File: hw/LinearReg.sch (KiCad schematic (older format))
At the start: 2 parts

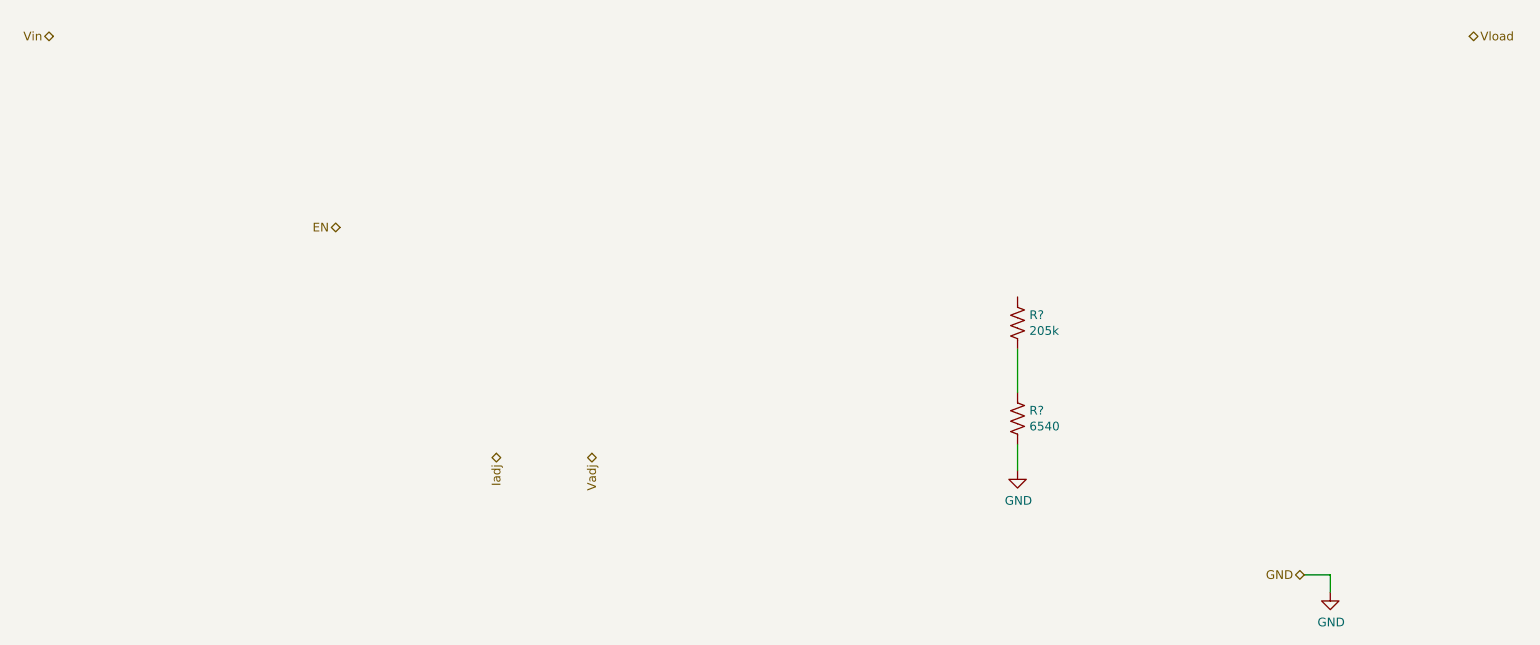
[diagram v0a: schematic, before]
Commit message: Primary SW component selection
selected some components for primary switcher, added AuxOut block, dropped down primary linear reg IC
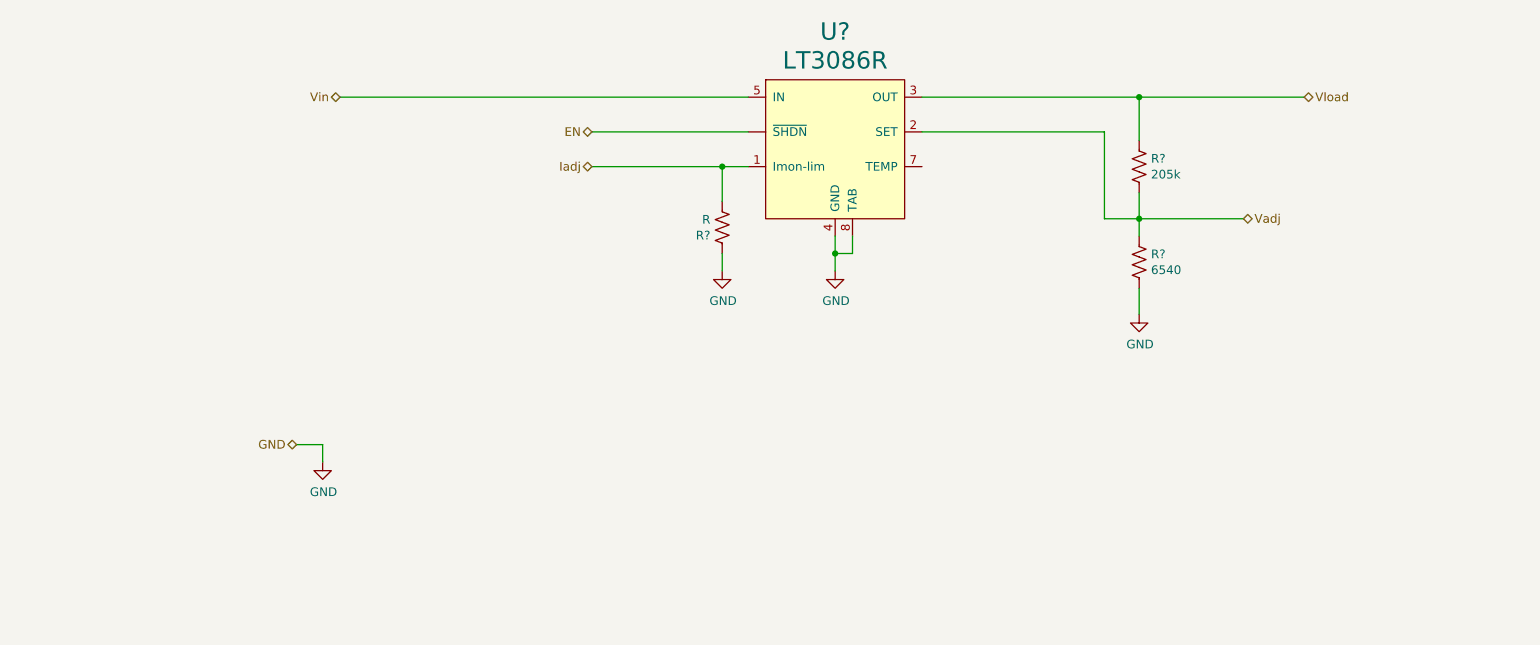
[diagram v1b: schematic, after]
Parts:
- added R?: R, Resistor_SMD:R_0603_1608Metric, symbol Device:R_US
- added U?: LT3086R, symbol RDSmith:LT3086R
- R? (x2): footprint (none) -> Resistor_SMD:R_0603_1608Metric
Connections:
- net EN: now also U?.~ (~SHDN)
- net GND: now also R?.1, U?.4 (GND), U?.8 (TAB)
- net Iadj: now also R?.2, U?.1 (Imon-lim)
- net Vadj: now also R?.1, R?.2, U?.2 (SET)
- net Vin: now also U?.5 (IN)
- net Vload: now also R?.1, U?.3 (OUT)
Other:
- moved on the sheet: R?
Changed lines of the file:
@@
 $Descr A4 11693 8268
 encoding utf-8
-Sheet 5 6
+Sheet 5 7
 Title ""
 Date ""
@@
 Comment4 ""
 $EndDescr
-Text HLabel 8750 4900 0    50   BiDi ~ 0
+Text HLabel 2950 4150 0    50   BiDi ~ 0
 GND
-Text HLabel 1550 1800 0    50   BiDi ~ 0
+Text HLabel 3200 2150 0    50   BiDi ~ 0
 Vin
-Text HLabel 9700 1800 2    50   BiDi ~ 0
+Text HLabel 8750 2150 2    50   BiDi ~ 0
 Vload
-Text HLabel 4650 4200 3    50   BiDi ~ 0
+Text HLabel 8400 2850 2    50   BiDi ~ 0
 Vadj
-Text HLabel 4100 4200 3    50   BiDi ~ 0
+Text HLabel 4650 2550 0    50   BiDi ~ 0
 Iadj
-Text HLabel 3200 2900 0    50   BiDi ~ 0
+Text HLabel 4650 2350 0    50   BiDi ~ 0
 EN
 $Comp
 L Device:R_US R?
 U 1 1 5E99EF91
-P 7100 3450
-F 0 "R?" H 7168 3496 50  0000 L CNN
-F 1 "205k" H 7168 3405 50  0000 L CNN
-F 2 "" V 7140 3440 50  0001 C CNN
-F 3 "~" H 7100 3450 50  0001 C CNN
-	1    7100 3450
+P 7800 2550
+F 0 "R?" H 7868 2596 50  0000 L CNN
+F 1 "205k" H 7868 2505 50  0000 L CNN
+F 2 "Resistor_SMD:R_0603_1608Metric" V 7840 2540 50  0001 C CNN
+F 3 "~" H 7800 2550 50  0001 C CNN
+	1    7800 2550
 	1    0    0    -1
 $EndComp
@@
 L Device:R_US R?
 U 1 1 5E99EFE9
-P 7100 4000
-F 0 "R?" H 7168 4046 50  0000 L CNN
-F 1 "6540" H 7168 3955 50  0000 L CNN
-F 2 "" V 7140 3990 50  0001 C CNN
-F 3 "~" H 7100 4000 50  0001 C CNN
-	1    7100 4000
+P 7800 3100
+F 0 "R?" H 7868 3146 50  0000 L CNN
+F 1 "6540" H 7868 3055 50  0000 L CNN
+F 2 "Resistor_SMD:R_0603_1608Metric" V 7840 3090 50  0001 C CNN
+F 3 "~" H 7800 3100 50  0001 C CNN
+	1    7800 3100
 	1    0    0    -1
 $EndComp
 Wire Wire Line
-	7100 3600 7100 3850
+	7800 2700 7800 2850
 $Comp
 L power:GND #PWR?
 U 1 1 5E99F06A
-P 8900 5000
-F 0 "#PWR?" H 8900 4750 50  0001 C CNN
-F 1 "GND" H 8905 4827 50  0000 C CNN
-F 2 "" H 8900 5000 50  0001 C CNN
-F 3 "" H 8900 5000 50  0001 C CNN
-	1    8900 5000
+P 3100 4250
+F 0 "#PWR?" H 3100 4000 50  0001 C CNN
+F 1 "GND" H 3105 4077 50  0000 C CNN
+F 2 "" H 3100 4250 50  0001 C CNN
+F 3 "" H 3100 4250 50  0001 C CNN
+	1    3100 4250
 	1    0    0    -1
 $EndComp
 Wire Wire Line
-	8900 5000 8900 4900
+	3100 4250 3100 4150
 Wire Wire Line
-	8900 4900 8750 4900
+	3100 4150 2950 4150
 $Comp
 L power:GND #PWR?
 U 1 1 5E99F090
-P 7100 4300
-F 0 "#PWR?" H 7100 4050 50  0001 C CNN
-F 1 "GND" H 7105 4127 50  0000 C CNN
-F 2 "" H 7100 4300 50  0001 C CNN
-F 3 "" H 7100 4300 50  0001 C CNN
-	1    7100 4300
+P 7800 3400
+F 0 "#PWR?" H 7800 3150 50  0001 C CNN
+F 1 "GND" H 7805 3227 50  0000 C CNN
+F 2 "" H 7800 3400 50  0001 C CNN
+F 3 "" H 7800 3400 50  0001 C CNN
+	1    7800 3400
 	1    0    0    -1
 $EndComp
 Wire Wire Line
-	7100 4300 7100 4150
+	7800 3400 7800 3250
+$Comp
+L RDSmith:LT3086R U?
+U 1 1 5EB6D3E5
+P 6050 2450
+F 0 "U?" H 6050 3127 100 0000 C CNN
+F 1 "LT3086R" H 6050 2961 100 0000 C CNN
+F 2 "" H 6050 2450 100 0001 C CNN
+F 3 "" H 6050 2450 100 0001 C CNN
+	1    6050 2450
+	1    0    0    -1
+$EndComp
+Wire Wire Line
+	8750 2150 7800 2150
+$Comp
+L power:GND #PWR?
+U 1 1 5EB6D471
+P 6050 3150
+F 0 "#PWR?" H 6050 2900 50  0001 C CNN
+F 1 "GND" H 6055 2977 50  0000 C CNN
+F 2 "" H 6050 3150 50  0001 C CNN
+F 3 "" H 6050 3150 50  0001 C CNN
+	1    6050 3150
+	1    0    0    -1
+$EndComp
+Wire Wire Line
+	6050 3150 6050 3050
+Wire Wire Line
+	6150 2950 6150 3050
+Wire Wire Line
+	6150 3050 6050 3050
+Connection ~ 6050 3050
+Wire Wire Line
+	6050 3050 6050 2950
+Wire Wire Line
+	3200 2150 5550 2150
+Wire Wire Line
+	4650 2350 5550 2350
+Wire Wire Line
+	7800 2400 7800 2150
+Connection ~ 7800 2150
+Wire Wire Line
+	7800 2150 6550 2150
+Wire Wire Line
+	6550 2350 7600 2350
+Wire Wire Line
+	7600 2350 7600 2850
+Wire Wire Line
+	7600 2850 7800 2850
+Connection ~ 7800 2850
+Wire Wire Line
+	7800 2850 7800 2950
+Wire Wire Line
+	8400 2850 7800 2850
+$Comp
+L Device:R_US R?
+U 1 1 5EB6DF74
+P 5400 2900
+F 0 "R?" H 5468 2946 50  0000 L CNN
+F 1 "R" H 5468 2855 50  0000 L CNN
+F 2 "Resistor_SMD:R_0603_1608Metric" V 5440 2890 50  0001 C CNN
+F 3 "~" H 5400 2900 50  0001 C CNN
+	1    5400 2900
+	-1   0    0    1
+$EndComp
+Wire Wire Line
+	5400 2750 5400 2550
+Wire Wire Line
+	5400 2550 5550 2550
+Wire Wire Line
+	4650 2550 5400 2550
+Connection ~ 5400 2550
+$Comp
+L power:GND #PWR?
+U 1 1 5EB6E351
+P 5400 3150
+F 0 "#PWR?" H 5400 2900 50  0001 C CNN
+F 1 "GND" H 5405 2977 50  0000 C CNN
+F 2 "" H 5400 3150 50  0001 C CNN
+F 3 "" H 5400 3150 50  0001 C CNN
+	1    5400 3150
+	1    0    0    -1
+$EndComp
+Wire Wire Line
+	5400 3150 5400 3050
 $EndSCHEMATC

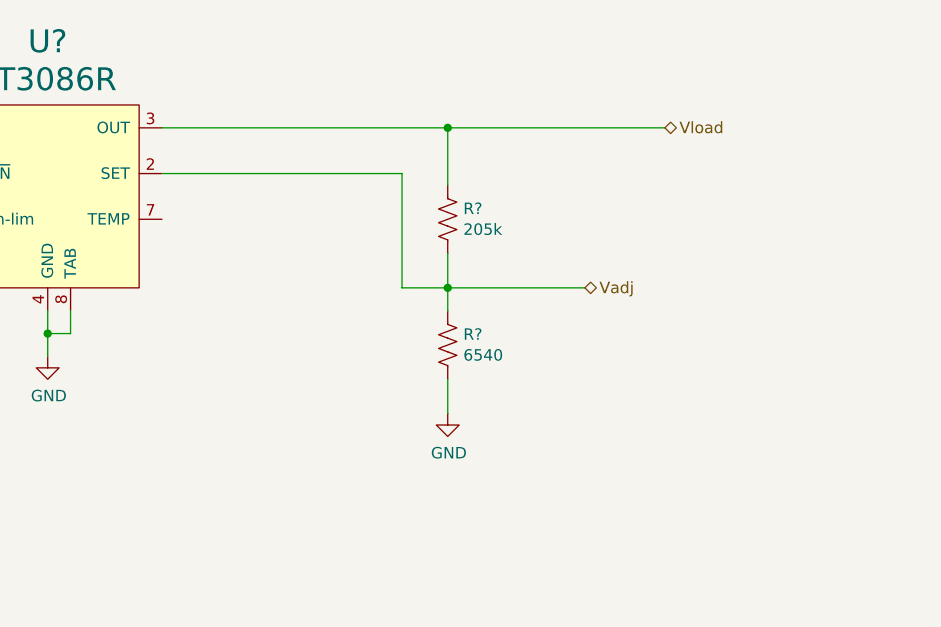
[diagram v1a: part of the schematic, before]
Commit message: Cap selections
Lots of capacitor selections & datasheet downloads

Updated LTPowerCAD model with initial compensation values for primary switcher
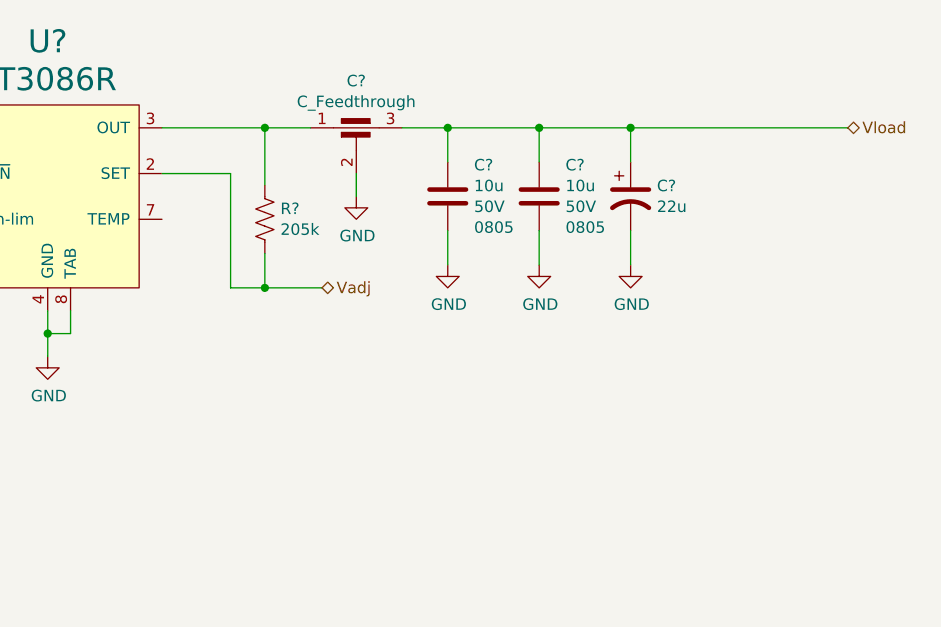
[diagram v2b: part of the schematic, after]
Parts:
- removed R?: 6540, Resistor_SMD:R_0603_1608Metric, symbol Device:R_US
- added C?: 22u, symbol Device:CP1
- added C?: C_Feedthrough, symbol Device:C_Feedthrough
- added C? (x2): 10u, Capacitor_SMD:C_0805_2012Metric_Pad1.15x1.40mm_HandSolder, symbol Device:C
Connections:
- net GND: now also C?.2, C?.2, C?.2, C?.2
- net Vload: now also C?.1, C?.1, C?.1, C?.3; no longer R?.1, U?.3 (OUT)
- new net: C?.1, R?.1, U?.3 (OUT)
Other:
- moved on the sheet: R?
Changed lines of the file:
@@
 Text HLabel 3200 2150 0    50   BiDi ~ 0
 Vin
-Text HLabel 8750 2150 2    50   BiDi ~ 0
+Text HLabel 9550 2150 2    50   BiDi ~ 0
 Vload
-Text HLabel 8400 2850 2    50   BiDi ~ 0
+Text HLabel 7250 2850 2    50   BiDi ~ 0
 Vadj
 Text HLabel 4650 2550 0    50   BiDi ~ 0
@@
 L Device:R_US R?
 U 1 1 5E99EF91
-P 7800 2550
-F 0 "R?" H 7868 2596 50  0000 L CNN
-F 1 "205k" H 7868 2505 50  0000 L CNN
-F 2 "Resistor_SMD:R_0603_1608Metric" V 7840 2540 50  0001 C CNN
-F 3 "~" H 7800 2550 50  0001 C CNN
-	1    7800 2550
-	1    0    0    -1
-$EndComp
-$Comp
-L Device:R_US R?
-U 1 1 5E99EFE9
-P 7800 3100
-F 0 "R?" H 7868 3146 50  0000 L CNN
-F 1 "6540" H 7868 3055 50  0000 L CNN
-F 2 "Resistor_SMD:R_0603_1608Metric" V 7840 3090 50  0001 C CNN
-F 3 "~" H 7800 3100 50  0001 C CNN
-	1    7800 3100
-	1    0    0    -1
-$EndComp
-Wire Wire Line
-	7800 2700 7800 2850
+P 7000 2550
+F 0 "R?" H 7068 2596 50  0000 L CNN
+F 1 "205k" H 7068 2505 50  0000 L CNN
+F 2 "Resistor_SMD:R_0603_1608Metric" V 7040 2540 50  0001 C CNN
+F 3 "~" H 7000 2550 50  0001 C CNN
+	1    7000 2550
+	1    0    0    -1
+$EndComp
+Wire Wire Line
+	7000 2700 7000 2850
 $Comp
 L power:GND #PWR?
@@
 Wire Wire Line
 	3100 4150 2950 4150
-$Comp
-L power:GND #PWR?
-U 1 1 5E99F090
-P 7800 3400
-F 0 "#PWR?" H 7800 3150 50  0001 C CNN
-F 1 "GND" H 7805 3227 50  0000 C CNN
-F 2 "" H 7800 3400 50  0001 C CNN
-F 3 "" H 7800 3400 50  0001 C CNN
-	1    7800 3400
-	1    0    0    -1
-$EndComp
-Wire Wire Line
-	7800 3400 7800 3250
 $Comp
 L RDSmith:LT3086R U?
@@
 	1    0    0    -1
 $EndComp
-Wire Wire Line
-	8750 2150 7800 2150
 $Comp
 L power:GND #PWR?
@@
 	4650 2350 5550 2350
 Wire Wire Line
-	7800 2400 7800 2150
-Connection ~ 7800 2150
-Wire Wire Line
-	7800 2150 6550 2150
-Wire Wire Line
-	6550 2350 7600 2350
-Wire Wire Line
-	7600 2350 7600 2850
-Wire Wire Line
-	7600 2850 7800 2850
-Connection ~ 7800 2850
-Wire Wire Line
-	7800 2850 7800 2950
-Wire Wire Line
-	8400 2850 7800 2850
+	7000 2400 7000 2150
+Wire Wire Line
+	7000 2150 6550 2150
+Wire Wire Line
+	6550 2350 6850 2350
+Wire Wire Line
+	6850 2350 6850 2850
+Wire Wire Line
+	6850 2850 7000 2850
+Connection ~ 7000 2850
+Wire Wire Line
+	7250 2850 7000 2850
 $Comp
 L Device:R_US R?
@@
 Wire Wire Line
 	5400 3150 5400 3050
+$Comp
+L Device:CP1 C?
+U 1 1 5EB6F187
+P 8600 2450
+F 0 "C?" H 8715 2496 50  0000 L CNN
+F 1 "22u" H 8715 2405 50  0000 L CNN
+F 2 "" H 8600 2450 50  0001 C CNN
+F 3 "~" H 8600 2450 50  0001 C CNN
+	1    8600 2450
+	1    0    0    -1
+$EndComp
+$Comp
+L Device:C_Feedthrough C?
+U 1 1 5EB6F1D6
+P 7400 2250
+F 0 "C?" H 7400 2555 50  0000 C CNN
+F 1 "C_Feedthrough" H 7400 2464 50  0000 C CNN
+F 2 "" V 7400 2250 50  0001 C CNN
+F 3 "~" V 7400 2250 50  0001 C CNN
+	1    7400 2250
+	1    0    0    -1
+$EndComp
+Wire Wire Line
+	7600 2150 7800 2150
+Wire Wire Line
+	7200 2150 7000 2150
+Connection ~ 7000 2150
+Wire Wire Line
+	7800 2300 7800 2150
+Connection ~ 7800 2150
+Wire Wire Line
+	7800 2150 8200 2150
+Wire Wire Line
+	8200 2300 8200 2150
+Connection ~ 8200 2150
+Wire Wire Line
+	8200 2150 8600 2150
+Wire Wire Line
+	8600 2300 8600 2150
+Connection ~ 8600 2150
+Wire Wire Line
+	8600 2150 9550 2150
+$Comp
+L power:GND #PWR?
+U 1 1 5EB7031E
+P 7800 2750
+F 0 "#PWR?" H 7800 2500 50  0001 C CNN
+F 1 "GND" H 7805 2577 50  0000 C CNN
+F 2 "" H 7800 2750 50  0001 C CNN
+F 3 "" H 7800 2750 50  0001 C CNN
+	1    7800 2750
+	1    0    0    -1
+$EndComp
+$Comp
+L power:GND #PWR?
+U 1 1 5EB70337
+P 8200 2750
+F 0 "#PWR?" H 8200 2500 50  0001 C CNN
+F 1 "GND" H 8205 2577 50  0000 C CNN
+F 2 "" H 8200 2750 50  0001 C CNN
+F 3 "" H 8200 2750 50  0001 C CNN
+	1    8200 2750
+	1    0    0    -1
+$EndComp
+$Comp
+L power:GND #PWR?
+U 1 1 5EB7036F
+P 8600 2750
+F 0 "#PWR?" H 8600 2500 50  0001 C CNN
+F 1 "GND" H 8605 2577 50  0000 C CNN
+F 2 "" H 8600 2750 50  0001 C CNN
+F 3 "" H 8600 2750 50  0001 C CNN
+	1    8600 2750
+	1    0    0    -1
+$EndComp
+Wire Wire Line
+	8600 2750 8600 2600
+Wire Wire Line
+	8200 2750 8200 2600
+Wire Wire Line
+	7800 2600 7800 2750
+$Comp
+L Device:C C?
+U 1 1 5EB70D16
+P 7800 2450
+F 0 "C?" H 7915 2587 50  0000 L CNN
+F 1 "10u" H 7915 2496 50  0000 L CNN
+F 2 "Capacitor_SMD:C_0805_2012Metric_Pad1.15x1.40mm_HandSolder" H 7838 2300 50  0001 C CNN
+F 3 "~" H 7800 2450 50  0001 C CNN
+F 4 "Murata_GRM21BR61H106KE43L" H 7800 2450 50  0001 C CNN "MfrNum"
+F 5 "50V" H 7915 2405 50  0000 L CNN "VRating"
+F 6 "0805" H 7915 2314 50  0000 L CNN "Size"
+	1    7800 2450
+	1    0    0    -1
+$EndComp
+$Comp
+L power:GND #PWR?
+U 1 1 5EB70D3D
+P 7400 2450
+F 0 "#PWR?" H 7400 2200 50  0001 C CNN
+F 1 "GND" H 7405 2277 50  0000 C CNN
+F 2 "" H 7400 2450 50  0001 C CNN
+F 3 "" H 7400 2450 50  0001 C CNN
+	1    7400 2450
+	1    0    0    -1
+$EndComp
+Wire Wire Line
+	7400 2450 7400 2350
+$Comp
+L Device:C C?
+U 1 1 5EC16A54
+P 8200 2450
+F 0 "C?" H 8315 2587 50  0000 L CNN
+F 1 "10u" H 8315 2496 50  0000 L CNN
+F 2 "Capacitor_SMD:C_0805_2012Metric_Pad1.15x1.40mm_HandSolder" H 8238 2300 50  0001 C CNN
+F 3 "~" H 8200 2450 50  0001 C CNN
+F 4 "Murata_GRM21BR61H106KE43L" H 8200 2450 50  0001 C CNN "MfrNum"
+F 5 "50V" H 8315 2405 50  0000 L CNN "VRating"
+F 6 "0805" H 8315 2314 50  0000 L CNN "Size"
+	1    8200 2450
+	1    0    0    -1
+$EndComp
 $EndSCHEMATC

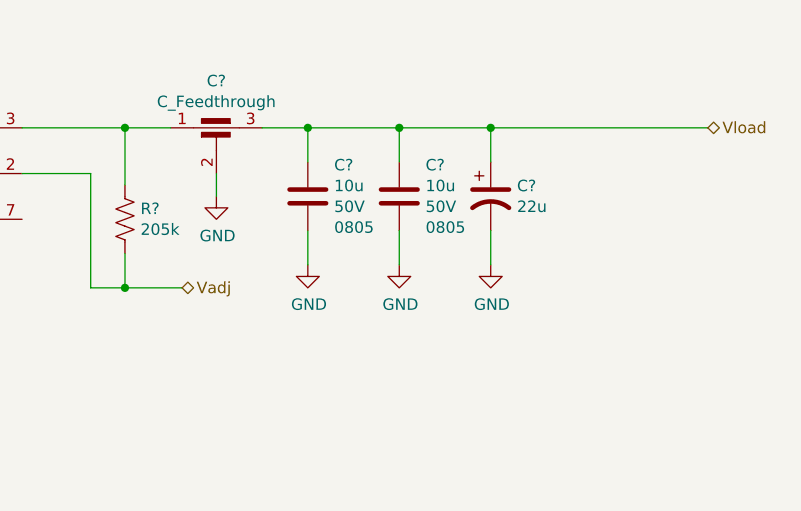
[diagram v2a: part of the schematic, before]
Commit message: more component selection
more caps selected; updated primary switcher sim file
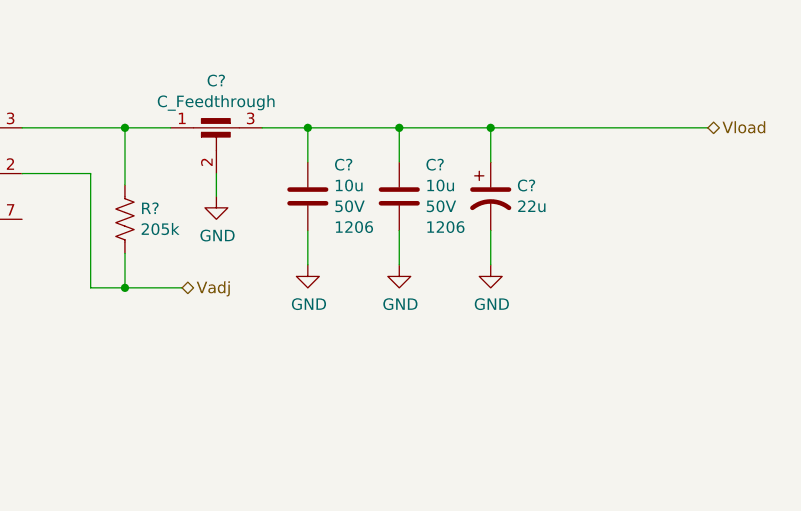
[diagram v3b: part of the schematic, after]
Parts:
- removed C?: 10u, Capacitor_SMD:C_0805_2012Metric_Pad1.15x1.40mm_HandSolder, symbol Device:C
- added C?: 10u, Capacitor_SMD:C_0805_2012Metric_Pad1.15x1.40mm_HandSolder, symbol Device:C
- C?: MfrNum Murata_GRM21BR61H106KE43L -> Murata_GRT31CR61H106ME01; Size 0805 -> 1206
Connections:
- net GND: now also C?.2
- net Vload: now also C?.1
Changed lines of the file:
@@
 F 2 "Capacitor_SMD:C_0805_2012Metric_Pad1.15x1.40mm_HandSolder" H 7838 2300 50  0001 C CNN
 F 3 "~" H 7800 2450 50  0001 C CNN
-F 4 "Murata_GRM21BR61H106KE43L" H 7800 2450 50  0001 C CNN "MfrNum"
+F 4 "Murata_GRT31CR61H106ME01" H 7800 2450 50  0001 C CNN "MfrNum"
 F 5 "50V" H 7915 2405 50  0000 L CNN "VRating"
-F 6 "0805" H 7915 2314 50  0000 L CNN "Size"
+F 6 "1206" H 7915 2314 50  0000 L CNN "Size"
 	1    7800 2450
 	1    0    0    -1
@@
 $Comp
 L Device:C C?
-U 1 1 5EC16A54
+U 1 1 5EB870A8
 P 8200 2450
 F 0 "C?" H 8315 2587 50  0000 L CNN
@@
 F 2 "Capacitor_SMD:C_0805_2012Metric_Pad1.15x1.40mm_HandSolder" H 8238 2300 50  0001 C CNN
 F 3 "~" H 8200 2450 50  0001 C CNN
-F 4 "Murata_GRM21BR61H106KE43L" H 8200 2450 50  0001 C CNN "MfrNum"
+F 4 "Murata_GRT31CR61H106ME01" H 8200 2450 50  0001 C CNN "MfrNum"
 F 5 "50V" H 8315 2405 50  0000 L CNN "VRating"
-F 6 "0805" H 8315 2314 50  0000 L CNN "Size"
+F 6 "1206" H 8315 2314 50  0000 L CNN "Size"
 	1    8200 2450
 	1    0    0    -1
